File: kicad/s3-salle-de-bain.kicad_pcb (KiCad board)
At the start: 2 copper layers, 145 x 108 mm, 23 parts, among them J1 Jack-3.5mm, J2 USB-C, Q1 AO3401, Q2 AO3401, SW1 EC11, SW2 Mute-SPDT, U1 ESP32-S3-DevKitC-1, U2 GY-PCM5102, U3 PAM8403, U4 INMP441, U5 AMS1117-3.3

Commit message: feat(cad): boitier v4 "galet" adapte a la carte 145x108 + 4 trous M3 PCB
Boitier 3D imprime entierement redessine pour s'adapter a la carte
porteuse KiCad (l'ancien cylindre Ø110 ne convenait pas).

Boitier (cad/boitier_v4/):
- galet rectangulaire arrondi (R28), design classe & epure
- 2 HP 40mm front-firing (grilles hexagonales + anneaux M2.5)
- molette centree : encodeur EC11 monte panneau (douille M7) +
  anneau LED WS2812 ; encodeur cable au PCB car l'axe 20mm ne peut
  atteindre le dessus situe ~50mm plus haut
- micro pinhole conique invisible
- fermeture par levre press-fit (aucune vis visible) + encoche demontage
- USB-C arriere, events de ventilation, pieds silicone
- parametrique (params.scad) ; STL + projet OrcaSlicer PA-CF (.3mf) fournis

PCB:
- ajout de 4 trous de fixation M3 (MK1-MK4) aux 4 points valides sans
  collision (find_mount_points.py), alignes sur les entretoises du boitier
- DRC: 0 violation

Co-Authored-By: Claude Opus 4.8 <noreply@anthropic.com>
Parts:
- added MK1: M3, MountingHole_3.2mm_M3, F.Cu at (7.00, 7.00)
- added MK2: M3, MountingHole_3.2mm_M3, F.Cu at (138.0, 44.0)
- added MK3: M3, MountingHole_3.2mm_M3, F.Cu at (104.0, 101.0)
- added MK4: M3, MountingHole_3.2mm_M3, F.Cu at (7.00, 101.0)

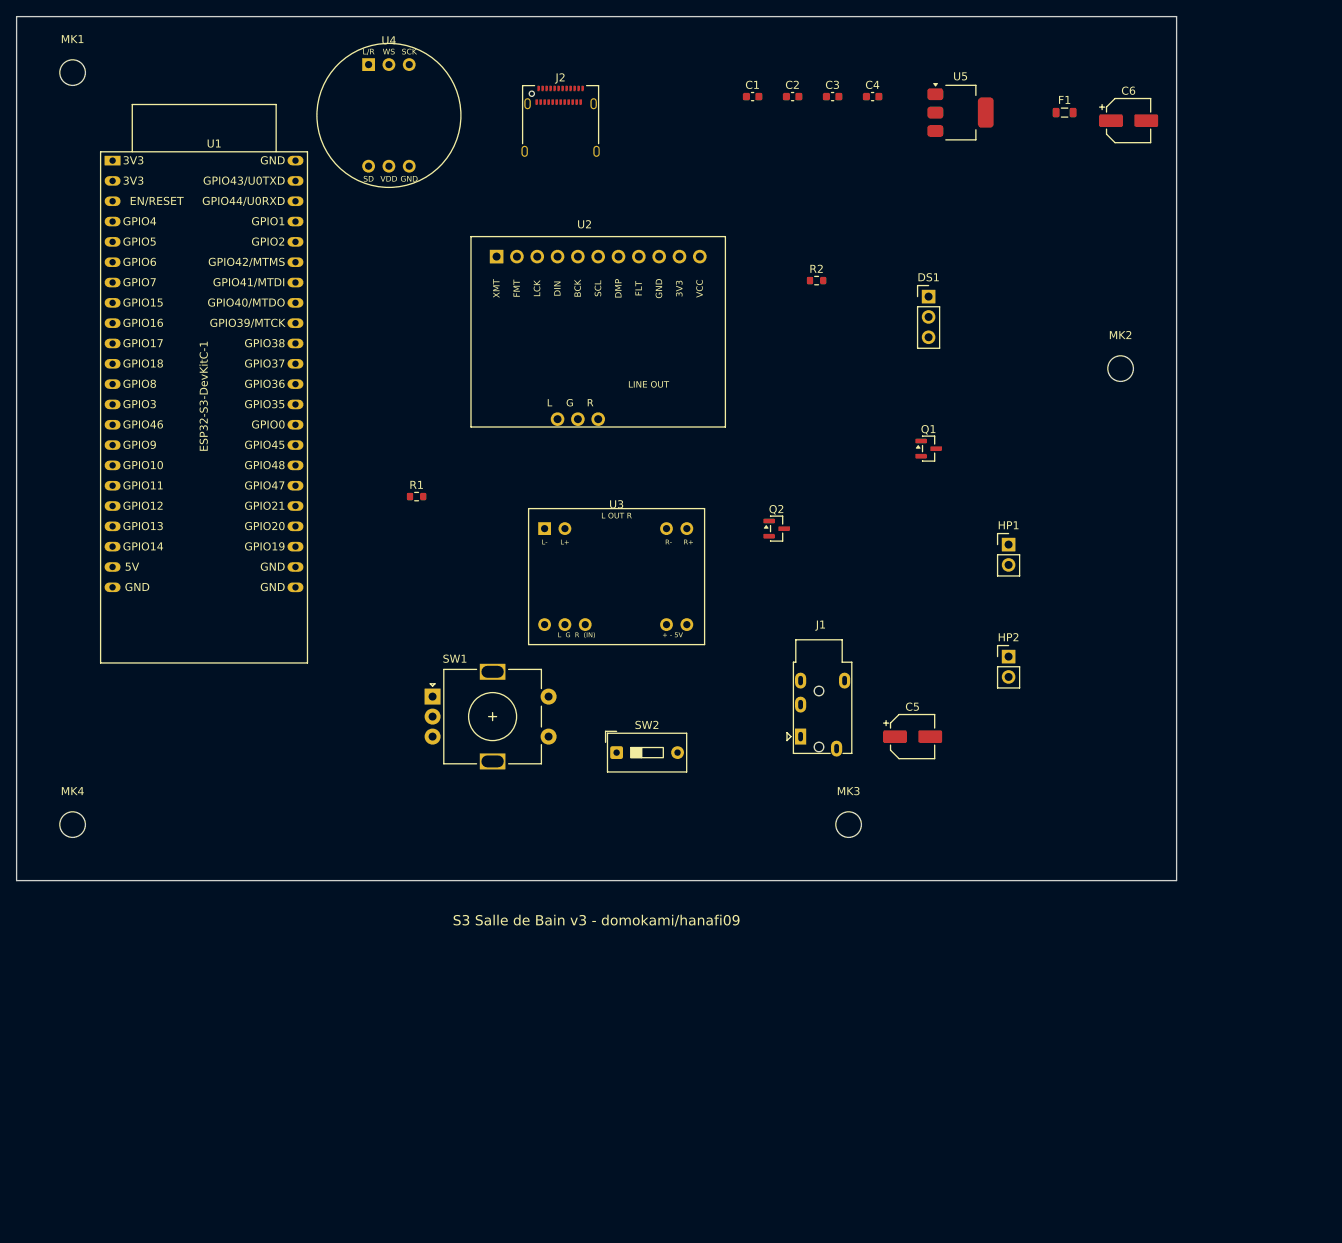
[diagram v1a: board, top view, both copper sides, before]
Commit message: docs: maj rapport technique PDF (boitier v4 + carte 76.7x108)
Meme mise a jour que le DOCX, cote PDF (ReportLab) :
- galet PA-CF 121x90x57 (au lieu du cylindre ABS Ø110)
- carte 76,7x108, entretoises sur trous MK1-MK4, USB-C sur J2
- 2 HP front-firing, molette EC11, fermeture press-fit
- CAO : v4_base/v4_top/v4_speaker_gasket (STL + STEP + .3mf)
- figures 4 et 5 = rendus CAO du galet v4
- chemin assets corrige (esp32_assets deplace)

Co-Authored-By: Claude Opus 4.8 <noreply@anthropic.com>
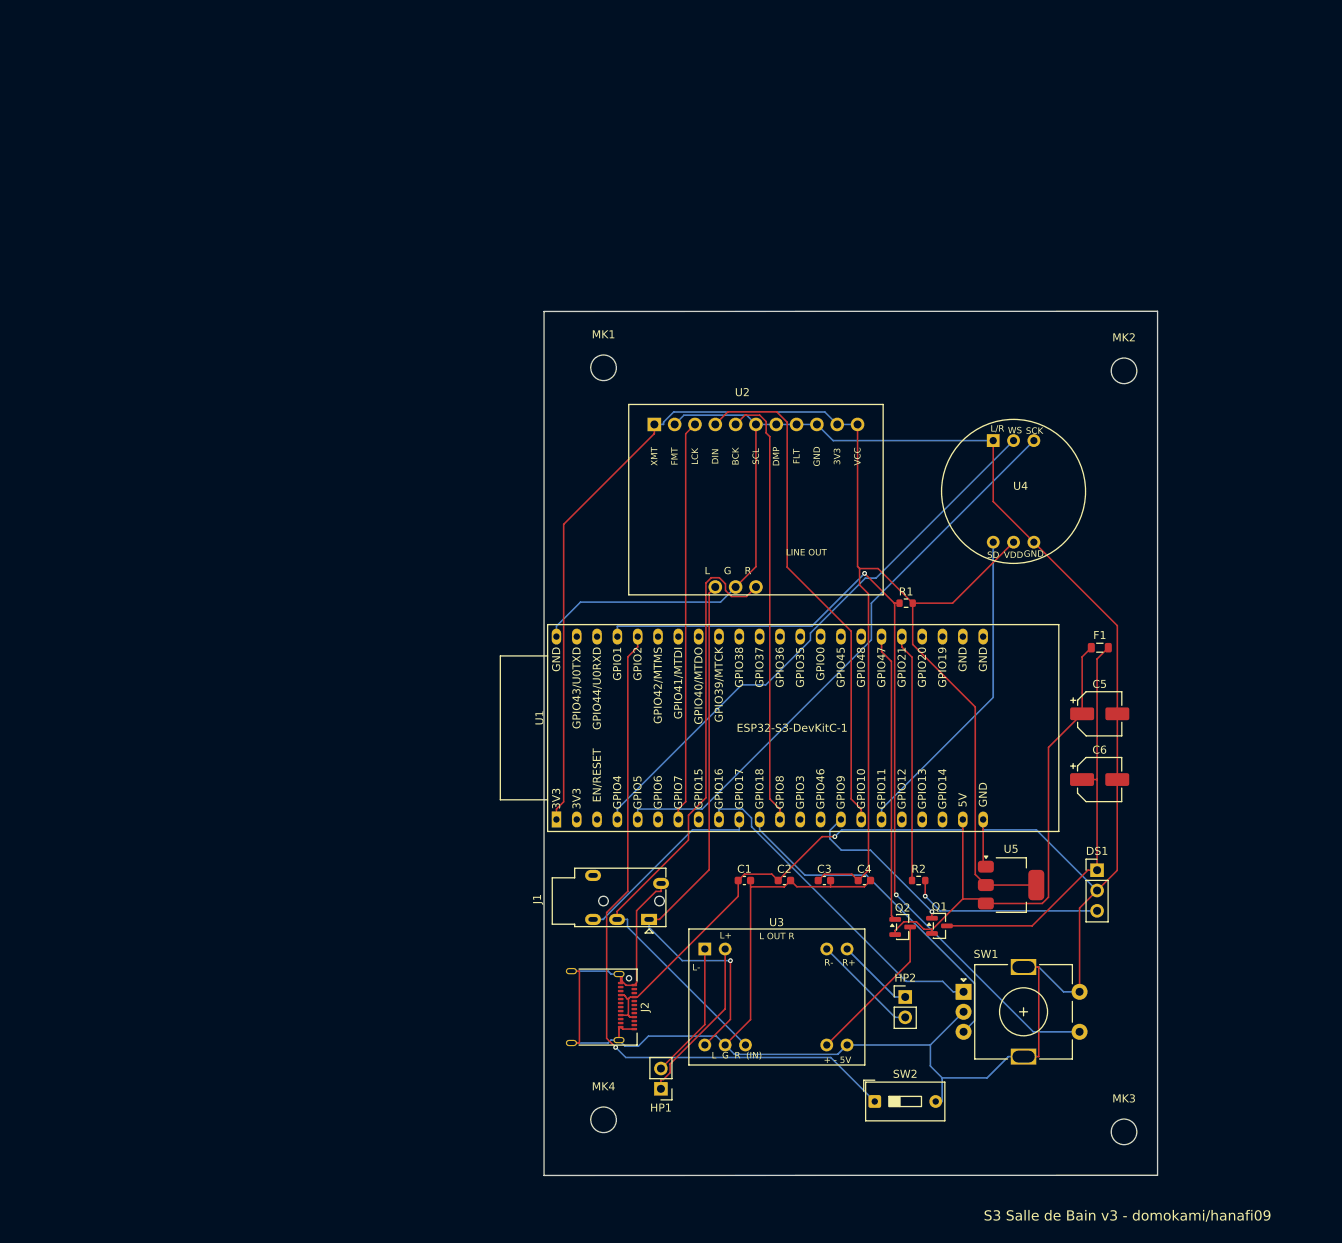
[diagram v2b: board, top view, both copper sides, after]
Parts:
- moved J2 109.9 mm to (72.2, 123.8), turned to -90 degrees
- moved U1 99.3 mm to (67.5, 100.4), turned to 90 degrees
- moved C1 98.0 mm to (91.0, 108.0)
- moved C2 98.0 mm to (96.0, 108.0)
- moved C3 98.0 mm to (101.0, 108.0)
- moved C4 98.0 mm to (106.0, 108.0)
- moved U5 96.8 mm to (124.3, 108.6)
- moved U4 91.1 mm to (122.1, 53.0)
- moved C6 82.4 mm to (135.4, 95.4)
- moved HP1 80.7 mm to (80.5, 134.0), turned to 180 degrees
- moved R2 76.1 mm to (112.8, 108.0)
- moved MK1 75.9 mm to (73.4, 43.9)
- moved MK4 75.9 mm to (73.4, 137.9)
- moved SW1 75.9 mm to (118.4, 121.9)
- moved DS1 74.7 mm to (135.1, 106.7)
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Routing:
- net GND: track 0.00 -> 364.6 mm
- net +3V3: track 0.00 -> 214.6 mm
- net +5V: track 0.00 -> 125.2 mm, vias 0 -> 1
- net BTN_CENTER: track 0.00 -> 107.4 mm, vias 0 -> 2
- net MUTE_SW: track 0.00 -> 88.6 mm, vias 0 -> 1
- net AUDIO_R: track 0.00 -> 78.2 mm
- net MIC_BCLK: track 0.00 -> 72.6 mm
- net AUDIO_L: track 0.00 -> 70.5 mm, vias 0 -> 1
- net MIC_LRCLK: track 0.00 -> 70.4 mm
- net DAC_DIN: track 0.00 -> 63.7 mm
- net DAC_BCK: track 0.00 -> 55.1 mm
- net +5V_LED: track 0.00 -> 51.9 mm
- net DAC_LRCK: track 0.00 -> 50.2 mm
- net ENC_B: track 0.00 -> 42.7 mm
- net ENC_A: track 0.00 -> 42.0 mm
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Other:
- board size 145 x 108 mm -> 76.7 x 108 mm
